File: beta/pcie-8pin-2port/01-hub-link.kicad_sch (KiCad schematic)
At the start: 6 parts, among them J1 TO-HUB

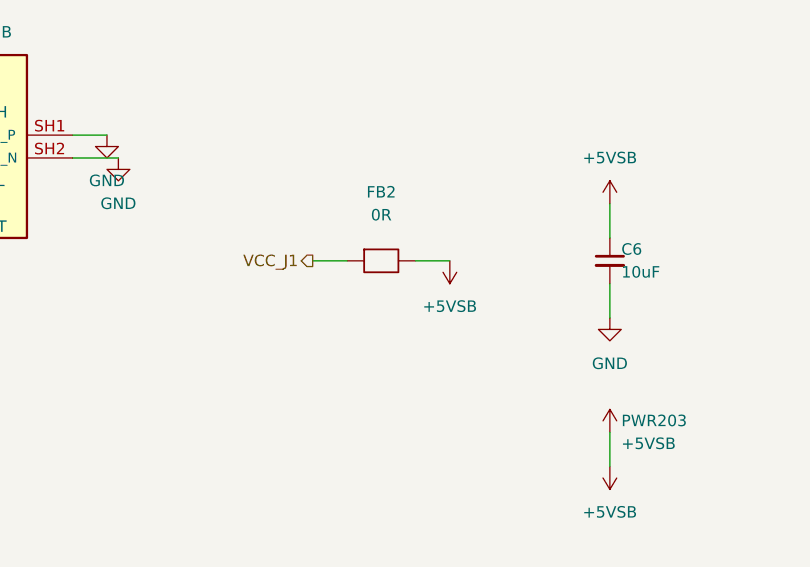
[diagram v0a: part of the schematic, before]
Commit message: pcie-8pin-2port: USB-ingress TPS2121 mux replaces the D2 SS34 ORing diode (spec v1.6.0 Sec 6.14)
Same package as the eps-8pin delta (docs/usb-ingress-bom-delta-2026-07-24.md Sec 3.2,
"Identical to the EPS delta"), adapted to this board's own real wiring, verified before
writing (not assumed from EPS): the raw connector-side node is named "VBUS_J5" here (not
"VBUS_RAW"), and FB1's own pin-1 stub rides a real (hierarchical_label ...) sheet-pin lane
up to the root sheet, not a plain label. Renaming that label in place while keeping the
hierarchical tag orphaned it (KiCad's hier_label_mismatch: "VBUS_F" has no matching sheet
pin) -- fixed by removing the hierarchical_label outright and replacing it with a plain
same-sheet label instead, since the new intermediate node has no reason to be externally
visible. D3/USBLC6 and D4/PESD5V0S1BA sit downstream of FB1 on this board (a real per-board
layout difference from EPS, not a defect) -- untouched either way. RJ-45-side pre-bead net
is "VCC_J1" (not "VCC_RJ45_RAW"); FB2's post-bead stub is the same plain +5VSB power-symbol
mechanism as EPS.

U4 = TPS2121RUXR: IN1 = the RJ-45 VCC feed after FB2, carried cross-sheet via a global_label
"VCC_RJ45" (01-hub-link.kicad_sch -> 07-usb-flash.kicad_sch); IN2 = VBUS behind new polyfuse
F1 inserted ahead of the existing FB1 bead; OUT = +5VSB. OV1/PR1 real dividers off IN1
(R15/R16, R17/R18); CP2/OV2/GND -> GND; ILIM (R14) and SS (C42) per the datasheet; ST (pin
9, "Output" type) left a genuine no_connect rather than hard-grounded, for the same reason
recorded in the EPS commit (grounding it puts two ERC-classified drivers on one net, a real
pin_to_pin ERROR). D2 removed entirely. Refdes shifted R13->R14.../C41->C42... (collision
with an unrelated existing 10k/100nF pair, same as EPS).

Gates: ERC 107->118, zero new errors (pin_not_driven=1 unchanged pre-existing), pin_to_pin
stays 53 (no new class), lib_symbol_mismatch +11 (new part types, same benign class).
Netlist-verified: +5VSB gain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
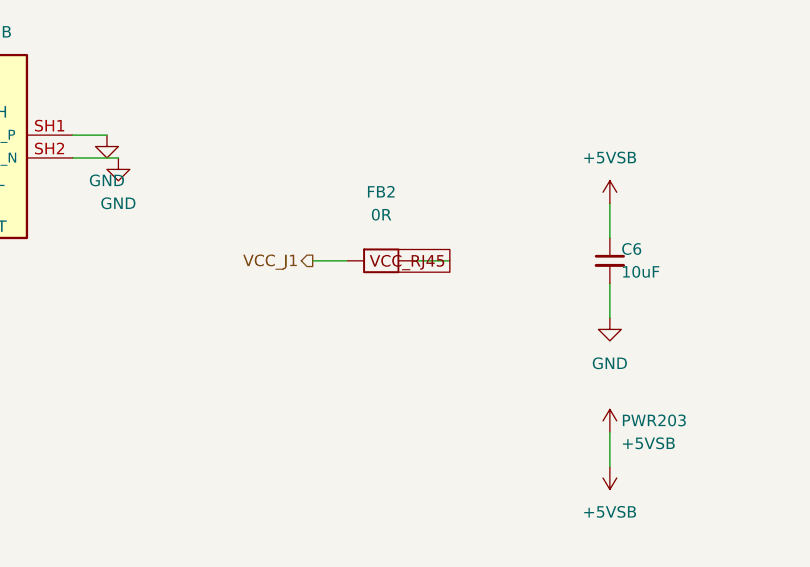
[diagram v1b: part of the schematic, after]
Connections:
- net +5VSB: no longer FB2.2
- new net VCC_RJ45: FB2.2
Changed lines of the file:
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@@
-	(symbol
-		(lib_id "cec-power:+5VSB")
-		(at 185.42 102.87 180)
-		(unit 1)
-		(exclude_from_sim no)
-		(in_bom yes)
-		(on_board yes)
-		(dnp no)
-		(property "Reference" "#PWR108" (at 185.42 100.33 0) (effects (font (size 1.27 1.27)) (hide yes)))
-		(property "Value" "+5VSB" (at 185.42 107.95 0) (effects (font (size 1.27 1.27))))
-		(pin "1")
-		(instances
-			(project "pcie8pin-2port-module"
-				(path "/a0c79a2e-4073-4d8d-b0bf-2c2ed1691f64/67f50ca3-8cb0-4aa6-9a3f-011faa4ff8d7" (reference "#PWR108") (unit 1))
-			)
-		)
-	)
 	(symbol
 		(lib_id "cec-power:+5VSB")
@@
 	(no_connect (at 123.19 91.44))
 	(no_connect (at 123.19 96.52))
+	(global_label "VCC_RJ45"
+		(shape passive)
+		(at 185.42 102.87 180)
+		(fields_autoplaced yes)
+		(effects (font (size 1.27 1.27)) (justify right bottom))
+		(property "Intersheetrefs" "${INTERSHEET_REFS}"
+			(at 185.42 102.87 0)
+			(effects (font (size 1.27 1.27)) (hide yes))
+		)
+	)
 	(sheet_instances
 		(path "/67f50ca3-8cb0-4aa6-9a3f-011faa4ff8d7"
